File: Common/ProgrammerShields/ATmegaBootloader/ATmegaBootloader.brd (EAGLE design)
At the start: 100 x 80 mm, 6 parts, among them J1 ARDUINO_R3_SHIELD

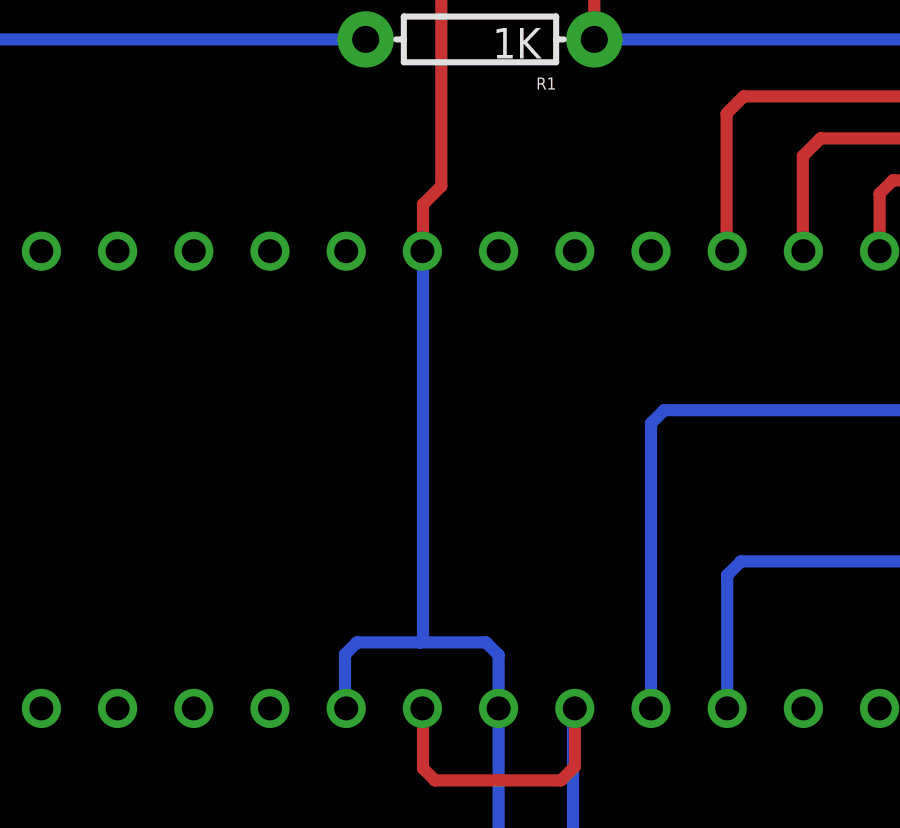
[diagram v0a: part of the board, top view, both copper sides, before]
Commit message: renamed our Arduino Shields folder
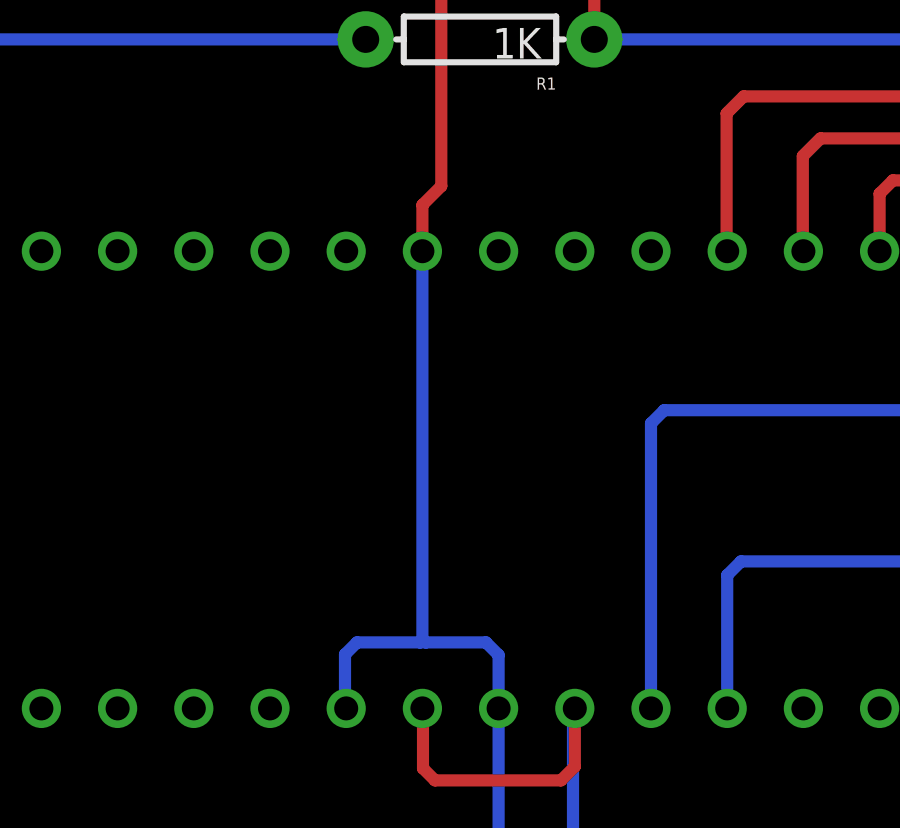
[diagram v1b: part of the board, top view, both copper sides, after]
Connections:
- new net RX: J1.RX
- new net TX: J1.TX
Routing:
- net GND: track 119.6 -> 119.7 mm, vias 1 -> 0
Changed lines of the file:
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@@
 <wire x1="43.75" y1="62.6" x2="41.21" y2="62.6" width="0.4064" layer="1"/>
 <wire x1="41.21" y1="62.6" x2="41.21" y2="48.41" width="0.4064" layer="1"/>
-<wire x1="41.21" y1="48.41" x2="40.6" y2="47.8" width="0.4064" layer="1"/>
-<wire x1="40.6" y1="47.8" x2="40.6" y2="46.26" width="0.4064" layer="1"/>
-<wire x1="40.6" y1="46.26" x2="40.58" y2="46.24" width="0.4064" layer="1"/>
+<wire x1="41.21" y1="48.41" x2="40.58" y2="47.78" width="0.4064" layer="1"/>
 <wire x1="43.12" y1="31" x2="43.12" y2="32.78" width="0.4064" layer="16"/>
 <wire x1="43.12" y1="32.78" x2="42.7" y2="33.2" width="0.4064" layer="16"/>
-<wire x1="42.7" y1="33.2" x2="40.5" y2="33.2" width="0.4064" layer="16"/>
+<wire x1="42.7" y1="33.2" x2="40.7" y2="33.2" width="0.4064" layer="16"/>
+<wire x1="40.7" y1="33.2" x2="40.5" y2="33.2" width="0.4064" layer="16"/>
 <wire x1="40.5" y1="33.2" x2="38.4" y2="33.2" width="0.4064" layer="16"/>
 <wire x1="38.4" y1="33.2" x2="38" y2="32.8" width="0.4064" layer="16"/>
 <wire x1="38" y1="32.8" x2="38" y2="31.04" width="0.4064" layer="16"/>
 <wire x1="38" y1="31.04" x2="38.04" y2="31" width="0.4064" layer="16"/>
-<via x="40.6" y="46.26" extent="1-16" drill="0.6"/>
-<wire x1="40.6" y1="46.26" x2="40.6" y2="33.3" width="0.4064" layer="16"/>
 <wire x1="40.6" y1="33.3" x2="40.5" y2="33.2" width="0.4064" layer="16"/>
 <wire x1="43.12" y1="31" x2="43.12" y2="21.08" width="0.4064" layer="16"/>
@@
 <wire x1="57.7" y1="16" x2="57.7" y2="14.36" width="0.4064" layer="1"/>
 <wire x1="57.7" y1="14.36" x2="57.72" y2="14.34" width="0.4064" layer="1"/>
+<wire x1="40.58" y1="46.24" x2="40.58" y2="33.32" width="0.4064" layer="16"/>
+<wire x1="40.58" y1="33.32" x2="40.7" y2="33.2" width="0.4064" layer="16"/>
+<wire x1="40.58" y1="46.24" x2="40.58" y2="47.78" width="0.4064" layer="1"/>
 </signal>
 <signal name="SCK">
@@
 <wire x1="70.16" y1="35.9" x2="70.2" y2="35.86" width="0.4064" layer="16"/>
 </signal>
+<signal name="RX">
+<contactref element="J1" pad="RX"/>
+</signal>
+<signal name="TX">
+<contactref element="J1" pad="TX"/>
+</signal>
 </signals>

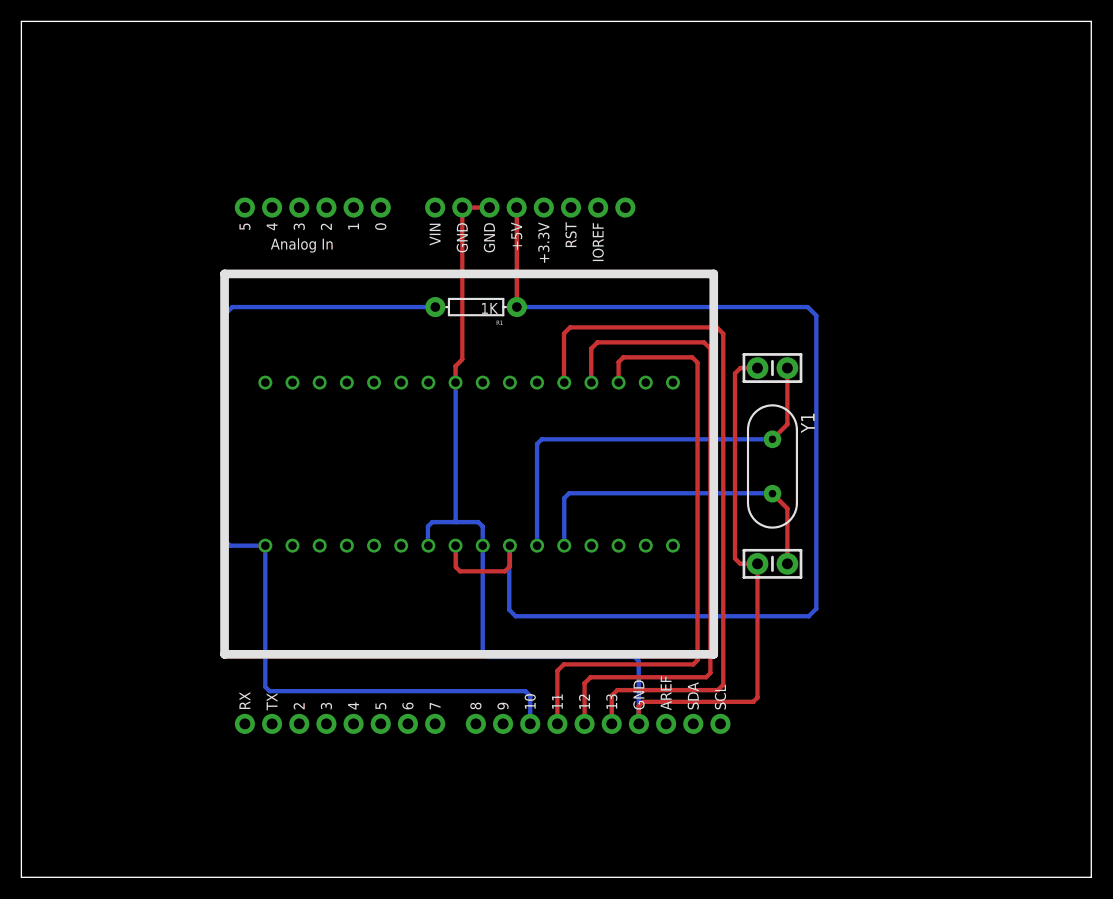
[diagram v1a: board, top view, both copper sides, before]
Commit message: Changed Schematic for ATmega programming shield
Added switch so board can be used for programming the bootloader and
normal programs
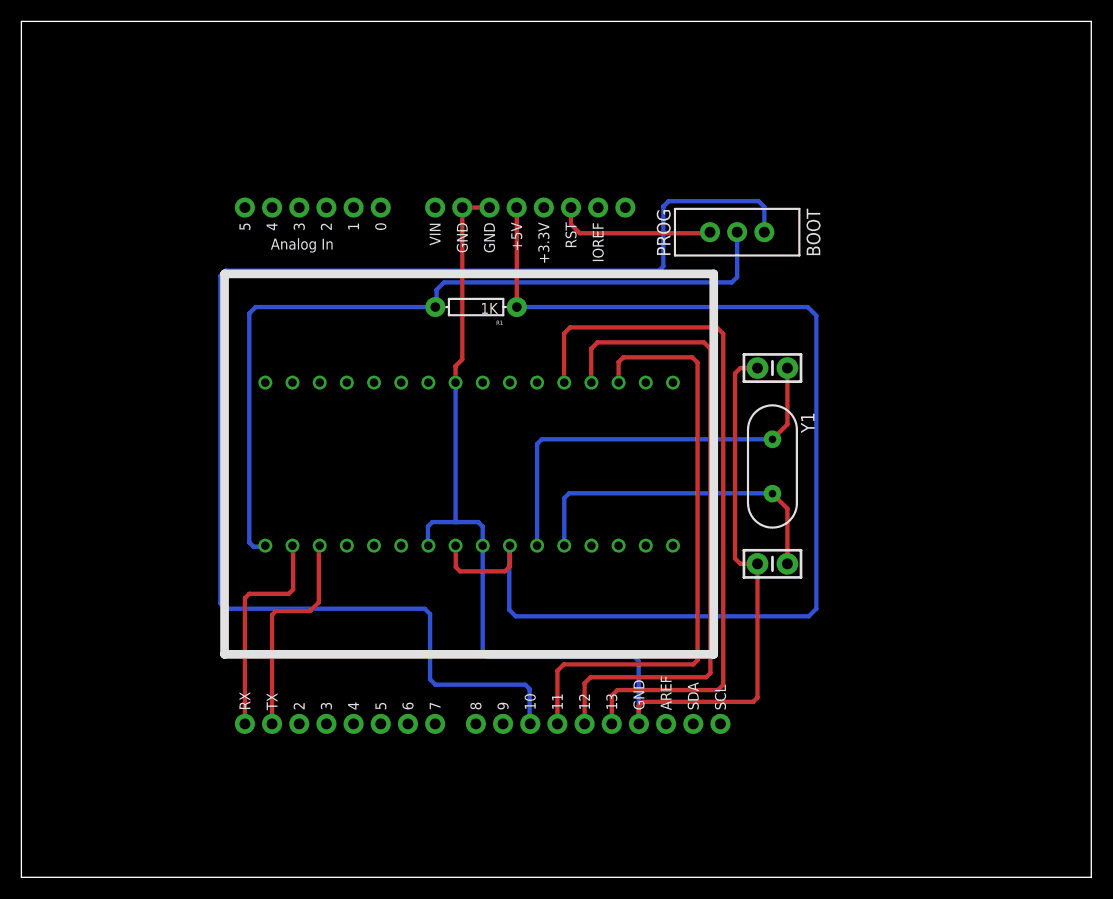
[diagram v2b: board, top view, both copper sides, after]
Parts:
- added RST-SW: (no value), SparkFun-Electromechanical:SWITCH-SPDT
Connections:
- new net RESET_BOOT: J1.D10, RST-SW.1
- new net RESET_PROG: J1.RES, RST-SW.3
- net RESET: now also RST-SW.2; no longer J1.D10
- net RX: now also U$1.30
- net TX: now also U$1.31
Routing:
- net RESET_BOOT: track 0.00 -> 129.3 mm
- net RX: track 0.00 -> 20.7 mm
- net TX: track 0.00 -> 20.4 mm
- net RESET_PROG: track 0.00 -> 14.9 mm
- net RESET: track 86.1 -> 75.2 mm
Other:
- board text added: "BOOT"
- board text added: "PROG"
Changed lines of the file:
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@@
 <?xml version="1.0" encoding="utf-8"?>
 <!DOCTYPE eagle SYSTEM "eagle.dtd">
-<eagle version="7.3.0">
+<eagle version="7.6.0">
 <drawing>
 <settings>
@@
 <layer number="116" name="Patch_BOT" color="9" fill="4" visible="no" active="yes"/>
 <layer number="118" name="Rect_Pads" color="7" fill="1" visible="yes" active="yes"/>
-<layer number="121" name="_tsilk" color="7" fill="1" visible="no" active="yes"/>
+<layer number="121" name="_tsilk" color="7" fill="1" visible="yes" active="yes"/>
 <layer number="122" name="_bsilk" color="7" fill="1" visible="no" active="yes"/>
 <layer number="123" name="tTestmark" color="7" fill="1" visible="no" active="yes"/>
@@
 <wire x1="100" y1="80" x2="0" y2="80" width="0" layer="20"/>
 <wire x1="0" y1="80" x2="0" y2="0" width="0" layer="20"/>
+<text x="73.4" y="62.5" size="1.27" layer="121" rot="R270">BOOT</text>
+<text x="59.4" y="62.5" size="1.27" layer="121" rot="R270">PROG</text>
 </plain>
 <attributes>
@@
 </element>
 <element name="U$1" library="MakerWear" package="TQFP32-BREAKOUT" value="ATMEGA-TQFP-BREAKOUT" x="60.9" y="31" rot="R90"/>
+<element name="RST-SW" library="SparkFun-Electromechanical" package="SWITCH-SPDT" value="" x="66.9" y="60.3" smashed="yes" rot="R270">
+<attribute name="PROD_ID" value="SWCH-08261" x="87.1" y="70.9" size="1.778" layer="27" rot="R270" display="off"/>
+<attribute name="VALUE" x="57.375" y="64.11" size="1.778" layer="27" ratio="10" rot="R270"/>
+</element>
 </elements>
 <signals>
@@
 <contactref element="U$1" pad="29"/>
 <contactref element="R1" pad="P$2"/>
-<contactref element="J1" pad="D10"/>
-<wire x1="47.56" y1="14.34" x2="47.56" y2="16.94" width="0.4064" layer="16"/>
-<wire x1="47.56" y1="16.94" x2="47.1" y2="17.4" width="0.4064" layer="16"/>
-<wire x1="47.1" y1="17.4" x2="23.2" y2="17.4" width="0.4064" layer="16"/>
-<wire x1="23.2" y1="17.4" x2="22.8" y2="17.8" width="0.4064" layer="16"/>
-<wire x1="22.8" y1="17.8" x2="22.8" y2="31" width="0.4064" layer="16"/>
-<wire x1="38.69" y1="53.3" x2="19.7" y2="53.3" width="0.4064" layer="16"/>
-<wire x1="19.7" y1="53.3" x2="18.9" y2="52.5" width="0.4064" layer="16"/>
-<wire x1="18.9" y1="52.5" x2="18.9" y2="31.6" width="0.4064" layer="16"/>
-<wire x1="18.9" y1="31.6" x2="19.5" y2="31" width="0.4064" layer="16"/>
-<wire x1="19.5" y1="31" x2="22.8" y2="31" width="0.4064" layer="16"/>
+<contactref element="RST-SW" pad="2"/>
+<wire x1="66.9" y1="60.3" x2="66.9" y2="56.1" width="0.4064" layer="16"/>
+<wire x1="66.9" y1="56.1" x2="66.4" y2="55.6" width="0.4064" layer="16"/>
+<wire x1="66.4" y1="55.6" x2="39.5" y2="55.6" width="0.4064" layer="16"/>
+<wire x1="39.5" y1="55.6" x2="38.8" y2="54.9" width="0.4064" layer="16"/>
+<wire x1="38.8" y1="54.9" x2="38.8" y2="53.41" width="0.4064" layer="16"/>
+<wire x1="38.8" y1="53.41" x2="38.69" y2="53.3" width="0.4064" layer="16"/>
+<wire x1="38.69" y1="53.3" x2="21.9" y2="53.3" width="0.4064" layer="16"/>
+<wire x1="21.9" y1="53.3" x2="21.3" y2="52.7" width="0.4064" layer="16"/>
+<wire x1="21.3" y1="52.7" x2="21.3" y2="31.3" width="0.4064" layer="16"/>
+<wire x1="21.3" y1="31.3" x2="21.7" y2="30.9" width="0.4064" layer="16"/>
+<wire x1="21.7" y1="30.9" x2="22.7" y2="30.9" width="0.4064" layer="16"/>
+<wire x1="22.7" y1="30.9" x2="22.8" y2="31" width="0.4064" layer="16"/>
 </signal>
 <signal name="VCC">
@@
 <signal name="RX">
 <contactref element="J1" pad="RX"/>
+<contactref element="U$1" pad="30"/>
+<wire x1="20.89" y1="14.34" x2="20.89" y2="26.09" width="0.4064" layer="1"/>
+<wire x1="20.89" y1="26.09" x2="21.3" y2="26.5" width="0.4064" layer="1"/>
+<wire x1="21.3" y1="26.5" x2="25" y2="26.5" width="0.4064" layer="1"/>
+<wire x1="25" y1="26.5" x2="25.4" y2="26.9" width="0.4064" layer="1"/>
+<wire x1="25.4" y1="26.9" x2="25.4" y2="30.94" width="0.4064" layer="1"/>
+<wire x1="25.4" y1="30.94" x2="25.34" y2="31" width="0.4064" layer="1"/>
 </signal>
 <signal name="TX">
 <contactref element="J1" pad="TX"/>
+<contactref element="U$1" pad="31"/>
+<wire x1="23.43" y1="14.34" x2="23.43" y2="24.53" width="0.4064" layer="1"/>
+<wire x1="23.43" y1="24.53" x2="23.8" y2="24.9" width="0.4064" layer="1"/>
+<wire x1="23.8" y1="24.9" x2="27" y2="24.9" width="0.4064" layer="1"/>
+<wire x1="27" y1="24.9" x2="27.8" y2="25.7" width="0.4064" layer="1"/>
+<wire x1="27.8" y1="25.7" x2="27.8" y2="30.92" width="0.4064" layer="1"/>
+<wire x1="27.8" y1="30.92" x2="27.88" y2="31" width="0.4064" layer="1"/>
+</signal>
+<signal name="RESET_BOOT">
+<contactref element="J1" pad="D10"/>
+<contactref element="RST-SW" pad="1"/>
+<wire x1="69.44" y1="60.3" x2="69.44" y2="62.66" width="0.4064" layer="16"/>
+<wire x1="69.44" y1="62.66" x2="68.9" y2="63.2" width="0.4064" layer="16"/>
+<wire x1="68.9" y1="63.2" x2="60.5" y2="63.2" width="0.4064" layer="16"/>
+<wire x1="60.5" y1="63.2" x2="60" y2="62.7" width="0.4064" layer="16"/>
+<wire x1="60" y1="62.7" x2="60" y2="57.1" width="0.4064" layer="16"/>
+<wire x1="60" y1="57.1" x2="59.6" y2="56.7" width="0.4064" layer="16"/>
+<wire x1="59.6" y1="56.7" x2="19.1" y2="56.7" width="0.4064" layer="16"/>
+<wire x1="19.1" y1="56.7" x2="18.6" y2="56.2" width="0.4064" layer="16"/>
+<wire x1="18.6" y1="56.2" x2="18.6" y2="25.6" width="0.4064" layer="16"/>
+<wire x1="18.6" y1="25.6" x2="19.1" y2="25.1" width="0.4064" layer="16"/>
+<wire x1="19.1" y1="25.1" x2="37.7" y2="25.1" width="0.4064" layer="16"/>
+<wire x1="37.7" y1="25.1" x2="38.2" y2="24.6" width="0.4064" layer="16"/>
+<wire x1="38.2" y1="24.6" x2="38.2" y2="18.5" width="0.4064" layer="16"/>
+<wire x1="38.2" y1="18.5" x2="38.7" y2="18" width="0.4064" layer="16"/>
+<wire x1="38.7" y1="18" x2="47.1" y2="18" width="0.4064" layer="16"/>
+<wire x1="47.1" y1="18" x2="47.5" y2="17.6" width="0.4064" layer="16"/>
+<wire x1="47.5" y1="17.6" x2="47.5" y2="14.4" width="0.4064" layer="16"/>
+<wire x1="47.5" y1="14.4" x2="47.56" y2="14.34" width="0.4064" layer="16"/>
+</signal>
+<signal name="RESET_PROG">
+<contactref element="J1" pad="RES"/>
+<contactref element="RST-SW" pad="3"/>
+<wire x1="51.37" y1="62.6" x2="51.37" y2="61.03" width="0.4064" layer="1"/>
+<wire x1="51.37" y1="61.03" x2="52.2" y2="60.2" width="0.4064" layer="1"/>
+<wire x1="52.2" y1="60.2" x2="64.26" y2="60.2" width="0.4064" layer="1"/>
+<wire x1="64.26" y1="60.2" x2="64.36" y2="60.3" width="0.4064" layer="1"/>
 </signal>
 </signals>
